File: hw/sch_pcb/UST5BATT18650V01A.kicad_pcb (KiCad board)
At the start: 2 copper layers, 90.9 x 72 mm, 14 parts, among them J1 SM03B-GHS-TB, J2 SM03B-GHS-TB, J3 SM03B-GHS-TB, J4 SM03B-GHS-TB

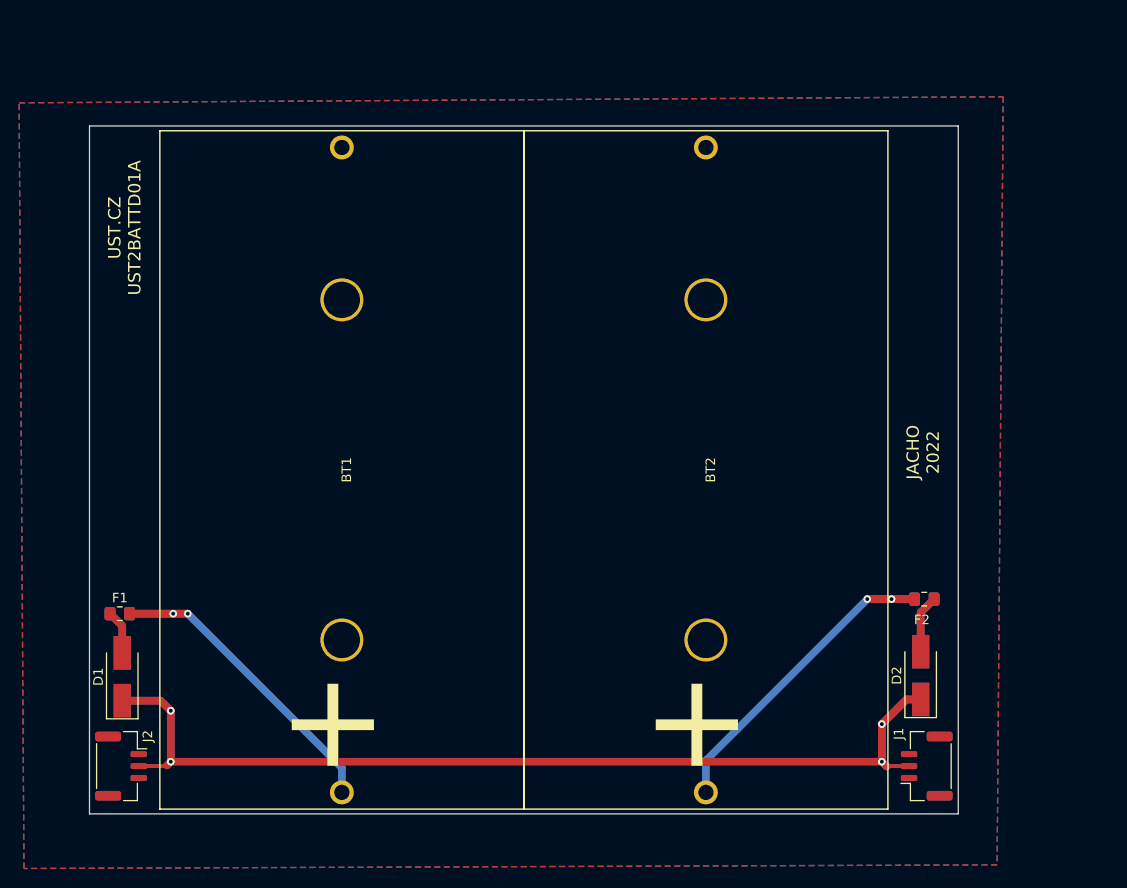
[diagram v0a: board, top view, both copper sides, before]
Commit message: Edit schema and PCB
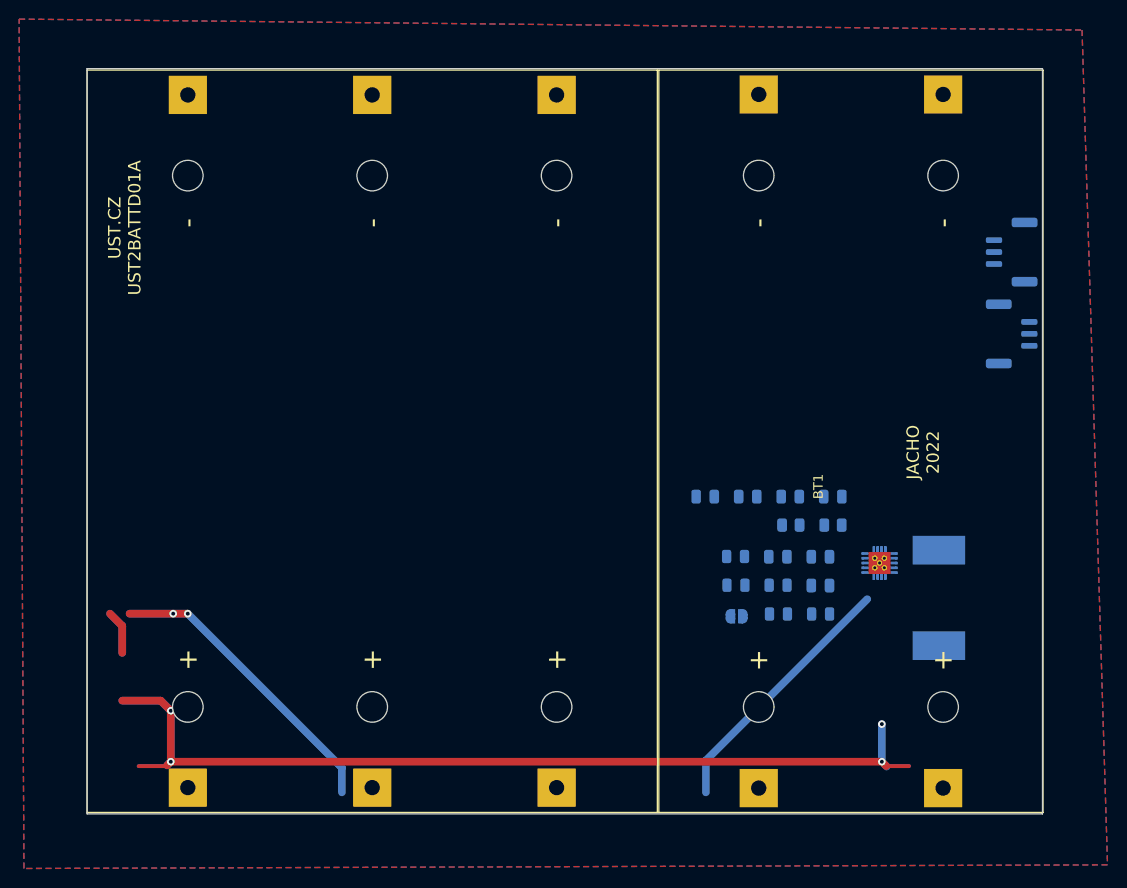
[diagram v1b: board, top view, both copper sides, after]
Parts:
- removed D1, D2, D3, D4: LSM115JE3/TR13, Diode_SMD:D_SMA_Handsoldering
- removed J3, J4: SM03B-GHS-TB, Connector_JST:JST_GH_SM03B-GHS-TB_1x03-1MP_P1.25mm_Horizontal
- added C1: 47uF/6V3, Capacitor_SMD:C_0805_2012Metric, B.Cu at (150.4, 118.3)
- added C2: 10uF, Capacitor_SMD:C_0805_2012Metric, B.Cu at (142.8, 109.0)
- added C3: 100nF, Capacitor_SMD:C_0805_2012Metric, B.Cu at (138.4, 109.0)
- added C4: 10p, Capacitor_SMD:C_0805_2012Metric, B.Cu at (151.7, 109.0)
- added C5: 10uF, Capacitor_SMD:C_0805_2012Metric, B.Cu at (147.3, 109.0)
- added C6: 47uF/6V3, Capacitor_SMD:C_0805_2012Metric, B.Cu at (150.4, 115.3)
- added C7: 47uF/6V3, Capacitor_SMD:C_0805_2012Metric, B.Cu at (146.0, 115.3)
- added F5: 100mA, Fuse:Fuse_0805_2012Metric, B.Cu at (141.5, 115.3)
- added JP1: SolderJumper_2_Open, Jumper:SolderJumper-2_P1.3mm_Open_RoundedPad1.0x1.5mm, B.Cu at (141.6, 121.6)
- added L1: DE1207-1, Mlab_L:DE1207, B.Cu at (162.8, 119.6)
- added R1: 560k, Resistor_SMD:R_0805_2012Metric, B.Cu at (147.3, 112.0)
- added R2: 100k, Resistor_SMD:R_0805_2012Metric, B.Cu at (151.7, 112.0)
- added X1: TPS63060, Package_SON:Texas_S-PWSON-N10_ThermalVias, B.Cu at (156.6, 116.0)
- BT1: value BX0037 -> NCR18650BL; footprint Mlab_Batery:BX0037 -> Mlab_Batery:BAT_BK-18650-PC4
- BT2: value BX0037 -> NCR18650BL; footprint Mlab_Batery:BX0037 -> Mlab_Batery:BAT_BK-18650-PC6
- F1, F2: value SR010-15 -> 100mA; footprint Fuse:Fuse_0805_2012Metric_Pad1.15x1.40mm_HandSolder -> Fuse:Fuse_0805_2012Metric; moved to B.Cu
- F3, F4: value SR010-15 -> 100mA; footprint Fuse:Fuse_0805_2012Metric_Pad1.15x1.40mm_HandSolder -> Fuse:Fuse_0805_2012Metric
- J1, J2: moved to B.Cu
- moved J2 103.6 mm to (170.4, 92.0), turned to 90 degrees
- moved F3 69.0 mm to (146.0, 118.3), turned to 180 degrees
- moved F1 64.6 mm to (141.6, 118.3), turned to 180 degrees
- moved J1 54.5 mm to (170.4, 83.4), turned to -90 degrees
- moved BT1 53.4 mm to (153.6, 103.2)
- moved BT2 35.1 mm to (103.5, 103.2)
- moved F4 15.3 mm to (146.0, 121.3)
- moved F2 11.0 mm to (150.4, 121.3)
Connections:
- net Net-(D1-Pad1) renamed +3V3
- F1 pad 1: Net-(D1-Pad2) -> Net-(C1-Pad2)
- F1 pad 2: Net-(F1-Pad2) -> Net-(BT1-Pad1+)
- F2 pad 1: Net-(D2-Pad2) -> Net-(C1-Pad2)
- F2 pad 2: Net-(F2-Pad2) -> Net-(BT1-Pad2+)
- F3 pad 1: Net-(D3-Pad2) -> Net-(C1-Pad2)
- F3 pad 2: Net-(F1-Pad2) -> Net-(BT2-Pad1+)
- F4 pad 1: Net-(D4-Pad2) -> Net-(C1-Pad2)
- F4 pad 2: Net-(F2-Pad2) -> Net-(BT2-Pad2+)
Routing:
- net +3V3: track 127.5 -> 0.00 mm, vias 4 -> 0
- net Net-(BT2-Pad1+): track 0.00 -> 113.3 mm, vias 0 -> 4
- net (no net): track 0.00 -> 74.1 mm, vias 0 -> 2
- net Net-(F1-Pad2): track 37.6 -> 0.00 mm, vias 2 -> 0
- net Net-(F2-Pad2): track 37.1 -> 0.00 mm, vias 2 -> 0
- net Net-(D4-Pad2): track 6.08 -> 0.00 mm
- net Net-(D2-Pad2): track 6.08 -> 0.00 mm
- net Net-(D3-Pad2): track 4.63 -> 0.00 mm
- net Net-(D1-Pad2): track 4.63 -> 0.00 mm
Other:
- board size 90.9 x 72 mm -> 100 x 78 mm

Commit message: Edit PCB
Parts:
- moved F3 59.2 mm to (89.9, 137.2), turned to -90 degrees
- moved F4 40.5 mm to (108.7, 137.2), turned to -90 degrees
- moved F5 25.7 mm to (128.0, 137.2), turned to -90 degrees
- moved F1 20.5 mm to (149.6, 137.2), turned to -90 degrees
- moved C2 18.8 mm to (153.9, 124.2)
- moved F2 17.2 mm to (157.2, 137.2), turned to -90 degrees
- moved C3 12.9 mm to (148.3, 117.2), turned to -90 degrees
- moved C7 9.45 mm to (153.9, 110.2)
- moved C1 9.11 mm to (153.9, 126.7)
- moved C5 8.82 mm to (153.9, 114.8)
- moved JP1 8.52 mm to (149.7, 124.2), turned to 0 degrees
- moved C4 5.55 mm to (150.0, 114.3)
- moved X1 5.36 mm to (152.6, 119.6), turned to 90 degrees
- moved C6 4.49 mm to (153.9, 112.5)
- moved R1 3.85 mm to (150.0, 109.2), turned to 0 degrees
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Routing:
- net Net-(BT2-Pad1+): track 113.3 -> 6.29 mm, vias 4 -> 0
- net Net-(C1-Pad2): track 0.00 -> 85.8 mm
- net (no net): track 74.1 -> 0.00 mm, vias 2 -> 6
- net +3V3: track 0.00 -> 56.1 mm
- net Net-(C4-Pad1): track 0.00 -> 10.4 mm
- net Net-(BT1-Pad2+): track 0.00 -> 6.63 mm
- net Net-(BT1-Pad1+): track 0.00 -> 6.24 mm
- net Net-(BT2-Pad3+): track 0.00 -> 5.79 mm
- net Net-(BT2-Pad2+): track 0.00 -> 5.78 mm
- net Net-(JP1-Pad2): track 0.00 -> 4.44 mm
- net Net-(C3-Pad2): track 0.00 -> 3.30 mm

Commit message: Edit PCB
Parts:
- added G1: LOGO_UST, MLAB_LOGA:UST, F.Cu at (94.6, 116.3)
- added G1: LOGO_UST, MLAB_LOGA:UST, B.Cu at (95.6, 116.5)
- moved C3 0.19 mm to (148.3, 117.3)
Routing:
- net GND: track 0.00 -> 16.9 mm, vias 0 -> 151
- net (no net): vias 6 -> 0
- added copper zone on B.Cu, net Net-(L1-Pad1)
- added copper zone on B.Cu, net Net-(L1-Pad2)
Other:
- board text added: "POWER OUT"
- board text added: "UST.CZ 2022"
- board text added: "UST.CZ UST5BATT18650V01A"
- board text removed: "UST.CZ UST2BATTD01A"

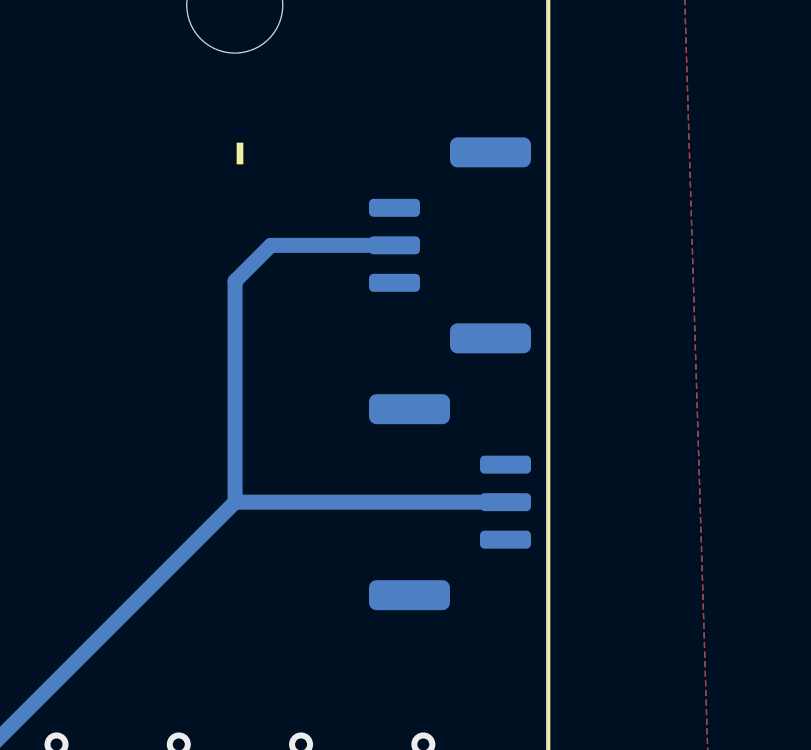
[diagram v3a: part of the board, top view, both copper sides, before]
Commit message: Edit schema and PCB
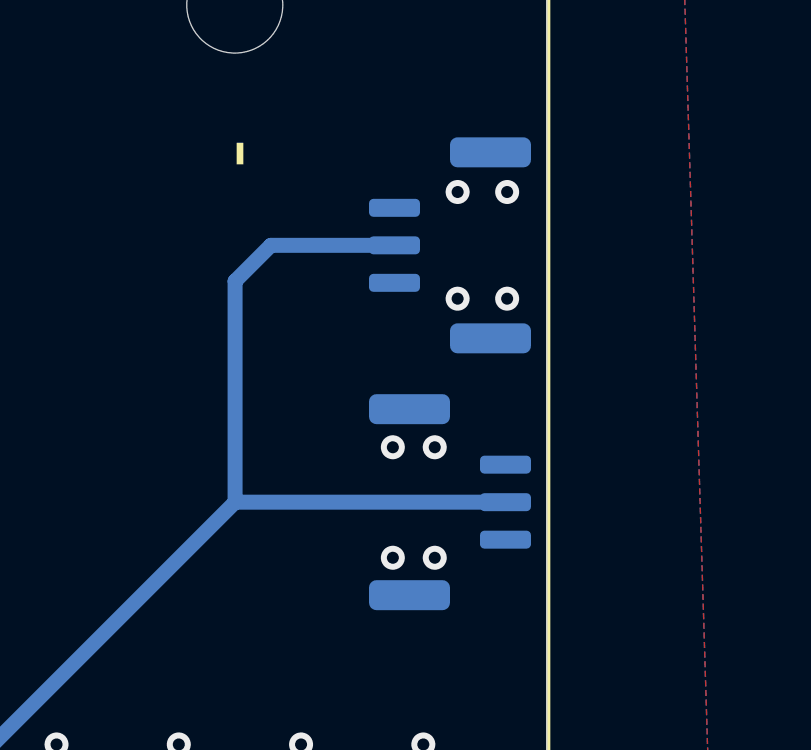
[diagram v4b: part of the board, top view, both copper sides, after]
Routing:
- net GND: vias 151 -> 159
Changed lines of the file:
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@@
   (via (at 118.364 140.208) (size 0.8) (drill 0.4) (layers "F.Cu" "B.Cu") (free) (net 1))
   (via (at 171.33455 128.524) (size 0.8) (drill 0.4) (layers "F.Cu" "B.Cu") (free) (net 1))
+  (via (at 168.529 90.17) (size 0.8) (drill 0.4) (layers "F.Cu" "B.Cu") (free) (net 1))
   (via (at 157.226 126.746) (size 0.8) (drill 0.4) (layers "F.Cu" "B.Cu") (free) (net 1))
   (via (at 85.748095 128.524) (size 0.8) (drill 0.4) (layers "F.Cu" "B.Cu") (free) (net 1))
@@
   (via (at 146.88127 128.524) (size 0.8) (drill 0.4) (layers "F.Cu" "B.Cu") (free) (net 1))
   (via (at 160.0835 120.015) (size 0.8) (drill 0.4) (layers "F.Cu" "B.Cu") (free) (net 1))
+  (via (at 170.688 85.217) (size 0.8) (drill 0.4) (layers "F.Cu" "B.Cu") (free) (net 1))
   (via (at 128.789545 100.076) (size 0.8) (drill 0.4) (layers "F.Cu" "B.Cu") (free) (net 1))
   (via (at 140.462 140.208) (size 0.8) (drill 0.4) (layers "F.Cu" "B.Cu") (free) (net 1))
@@
   (via (at 149.86 117.221) (size 0.8) (drill 0.4) (layers "F.Cu" "B.Cu") (free) (net 1))
   (via (at 157.226 125.73) (size 0.8) (drill 0.4) (layers "F.Cu" "B.Cu") (free) (net 1))
+  (via (at 168.529 93.853) (size 0.8) (drill 0.4) (layers "F.Cu" "B.Cu") (free) (net 1))
   (via (at 116.56291 100.076) (size 0.8) (drill 0.4) (layers "F.Cu" "B.Cu") (free) (net 1))
   (via (at 126.83836 70.612) (size 0.8) (drill 0.4) (layers "F.Cu" "B.Cu") (free) (net 1))
@@
   (via (at 147.574 112.268) (size 0.8) (drill 0.4) (layers "F.Cu" "B.Cu") (free) (net 1))
   (via (at 150.876 117.221) (size 0.8) (drill 0.4) (layers "F.Cu" "B.Cu") (free) (net 1))
+  (via (at 172.339 81.661) (size 0.8) (drill 0.4) (layers "F.Cu" "B.Cu") (free) (net 1))
   (via (at 149.733 116.332) (size 0.8) (drill 0.4) (layers "F.Cu" "B.Cu") (free) (net 1))
   (via (at 100.076 140.208) (size 0.8) (drill 0.4) (layers "F.Cu" "B.Cu") (free) (net 1))
@@
   (via (at 167.59382 70.612) (size 0.8) (drill 0.4) (layers "F.Cu" "B.Cu") (free) (net 1))
   (via (at 110.53618 70.612) (size 0.8) (drill 0.4) (layers "F.Cu" "B.Cu") (free) (net 1))
+  (via (at 172.339 85.217) (size 0.8) (drill 0.4) (layers "F.Cu" "B.Cu") (free) (net 1))
   (via (at 159.44272 70.612) (size 0.8) (drill 0.4) (layers "F.Cu" "B.Cu") (free) (net 1))
   (via (at 165.46945 100.076) (size 0.8) (drill 0.4) (layers "F.Cu" "B.Cu") (free) (net 1))
@@
   (via (at 139.064995 70.612) (size 0.8) (drill 0.4) (layers "F.Cu" "B.Cu") (free) (net 1))
   (via (at 159.107905 128.524) (size 0.8) (drill 0.4) (layers "F.Cu" "B.Cu") (free) (net 1))
+  (via (at 169.926 90.17) (size 0.8) (drill 0.4) (layers "F.Cu" "B.Cu") (free) (net 1))
   (via (at 88.392 140.208) (size 0.8) (drill 0.4) (layers "F.Cu" "B.Cu") (free) (net 1))
   (via (at 122.428 128.524) (size 0.8) (drill 0.4) (layers "F.Cu" "B.Cu") (free) (net 1))
@@
   (via (at 90.158455 70.612) (size 0.8) (drill 0.4) (layers "F.Cu" "B.Cu") (free) (net 1))
   (via (at 130.3655 140.208) (size 0.8) (drill 0.4) (layers "F.Cu" "B.Cu") (free) (net 1))
+  (via (at 169.926 93.853) (size 0.8) (drill 0.4) (layers "F.Cu" "B.Cu") (free) (net 1))
   (via (at 156.083 123.19) (size 0.8) (drill 0.4) (layers "F.Cu" "B.Cu") (free) (net 1))
   (via (at 79.883005 100.076) (size 0.8) (drill 0.4) (layers "F.Cu" "B.Cu") (free) (net 1))
@@
   (via (at 96.185185 100.076) (size 0.8) (drill 0.4) (layers "F.Cu" "B.Cu") (free) (net 1))
   (via (at 156.2735 119.126) (size 0.8) (drill 0.4) (layers "F.Cu" "B.Cu") (free) (net 1))
+  (via (at 170.688 81.661) (size 0.8) (drill 0.4) (layers "F.Cu" "B.Cu") (free) (net 1))
   (via (at 150.622 116.332) (size 0.8) (drill 0.4) (layers "F.Cu" "B.Cu") (free) (net 1))
   (via (at 155.03236 128.524) (size 0.8) (drill 0.4) (layers "F.Cu" "B.Cu") (free) (net 1))

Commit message: Edit PCB and schema
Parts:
- added F6: 1,1A, Mlab_F:1812, B.Cu at (154.3, 104.9)
- added R3: 20k, Resistor_SMD:R_0805_2012Metric, B.Cu at (150.0, 109.5)
- moved R1 2.03 mm to (150.0, 107.2)
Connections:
- C5 pad 2: +3V3 -> Net-(C5-Pad2)
- C6 pad 2: +3V3 -> Net-(C5-Pad2)
- C7 pad 2: +3V3 -> Net-(C5-Pad2)
- J1 pad 2: +3V3 -> VDD
- J2 pad 2: +3V3 -> VDD
- R1 pad 1: Net-(C4-Pad1) -> Net-(R1-Pad1)
- R1 pad 2: +3V3 -> Net-(C5-Pad2)
- X1 pad 9: +3V3 -> Net-(C5-Pad2)
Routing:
- net +3V3: track 56.1 -> 0.00 mm
- net VDD: track 0.00 -> 36.9 mm
- net Net-(C5-Pad2): track 0.00 -> 18.0 mm
- net Net-(R1-Pad1): track 0.00 -> 2.29 mm
- net Net-(C4-Pad1): track 10.4 -> 9.38 mm
- net GND: vias 159 -> 163
